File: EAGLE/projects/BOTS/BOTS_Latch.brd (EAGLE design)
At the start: 26.7 x 47 mm, 5 parts, among them J1 T821108A1S100CEU, K1 RT444012

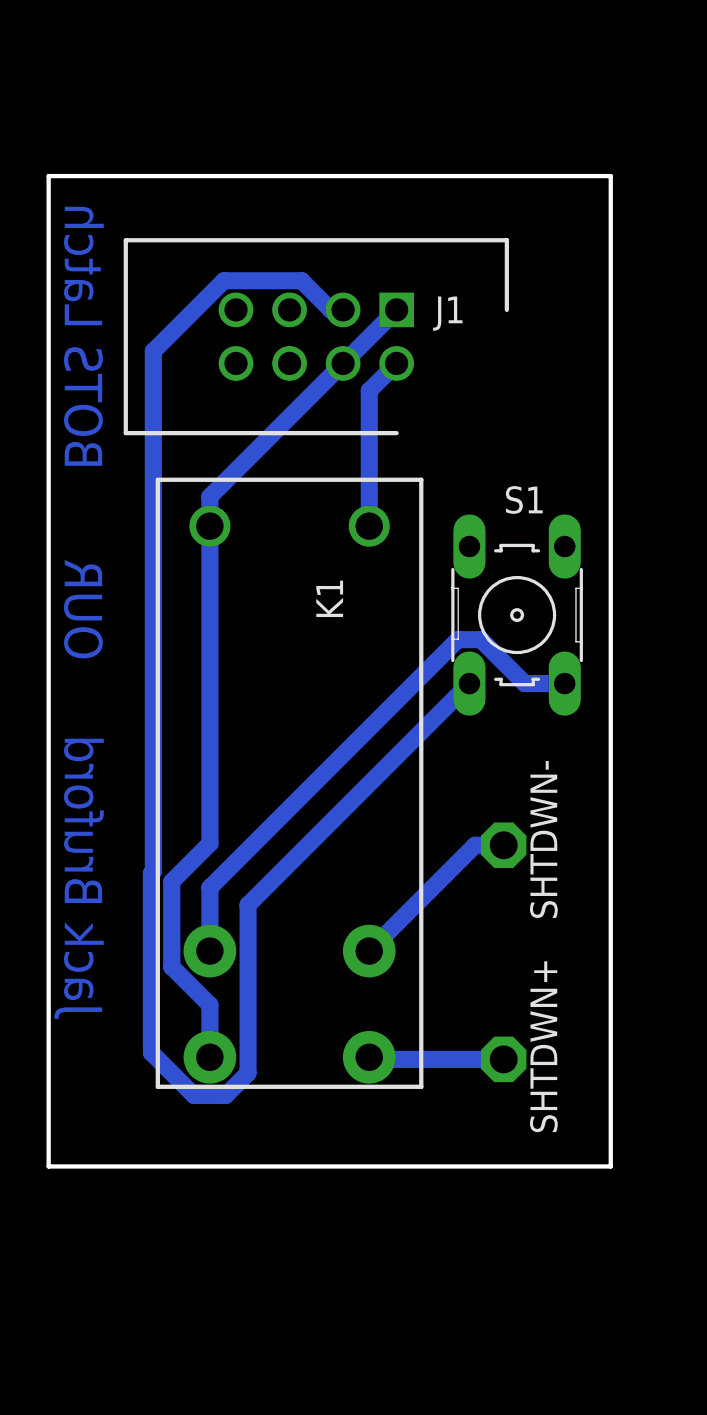
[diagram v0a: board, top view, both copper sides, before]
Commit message: Updates to BOTS circuit moving 12v pin to correct position and AMS circuit updates, including library for dual coil relay
Signed-off-by: Jack Bruford <jack.bruford41@gmail.com>
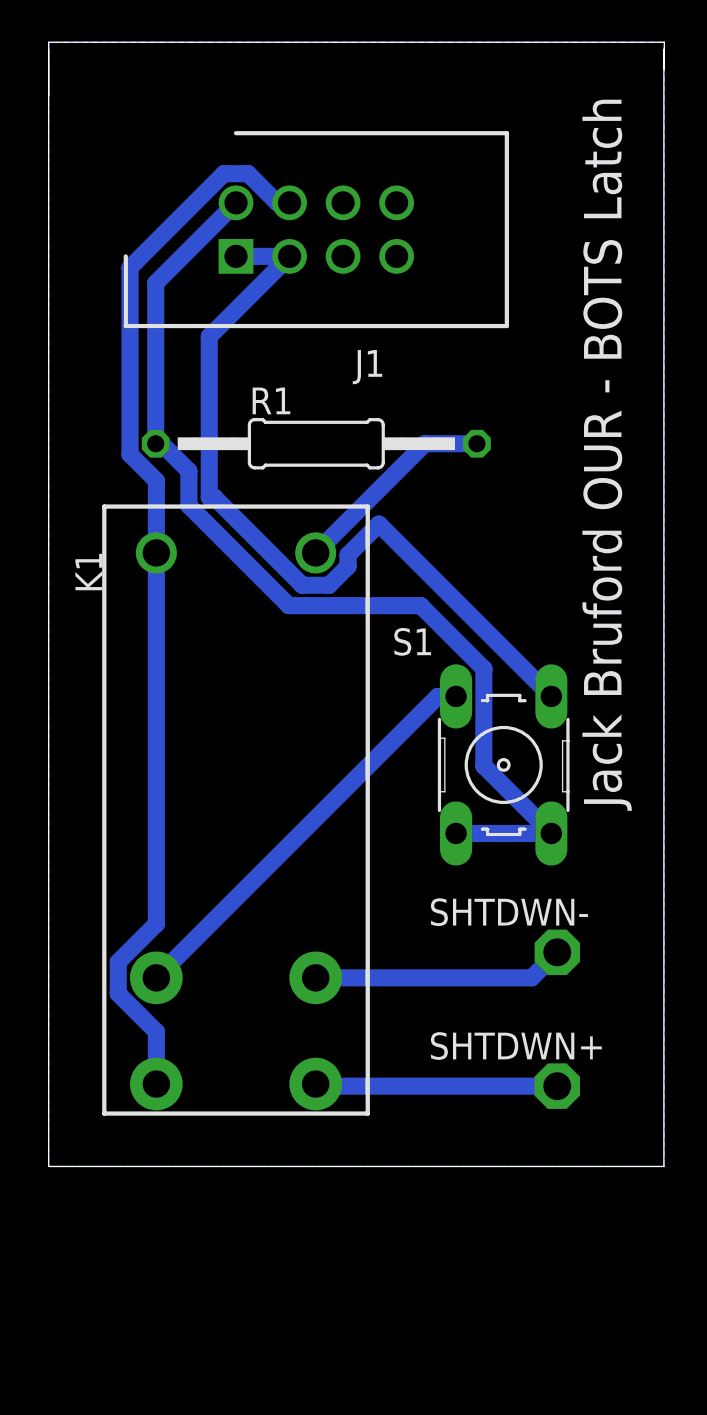
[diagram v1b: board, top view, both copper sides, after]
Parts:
- added R1: (no value), rcl:0207/15
- moved J1 8.03 mm to (8.89, 43.2), turned to 0 degrees
- moved S1 7.14 mm to (21.6, 19.1), turned to 90 degrees
- moved SHTDWN- 5.68 mm to (24.1, 10.2)
- moved K1 2.84 mm to (8.89, 16.5)
- moved SHTDWN+ 2.84 mm to (24.1, 3.81)
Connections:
- new net N$5: J1.4, K1.14, K1.A1
- net +12V: now also J1.3, S1.4; no longer J1.4, K1.14, K1.A1
- net GND: now also R1.1, S1.1, S1.3; no longer K1.A2
- net N$2: now also K1.A2, R1.2; no longer J1.3, S1.4
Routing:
- net N$2: track 73.0 -> 9.80 mm
- net N$5: track 0.00 -> 50.7 mm
- net GND: track 8.26 -> 47.6 mm
- net N$1: track 25.6 -> 19.7 mm
- net N$3: track 6.42 -> 11.5 mm
- net N$4: track 8.46 -> 12.0 mm
- net +12V: track 40.6 -> 38.4 mm
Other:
- board size 26.7 x 47 mm -> 29.2 x 53.3 mm
- board text added: "Jack Bruford OUR - BOTS Latch"
- board text removed: "Jack Bruford OUR BOTS Latch"

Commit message: BOTS revision so that ESDC goes through connector
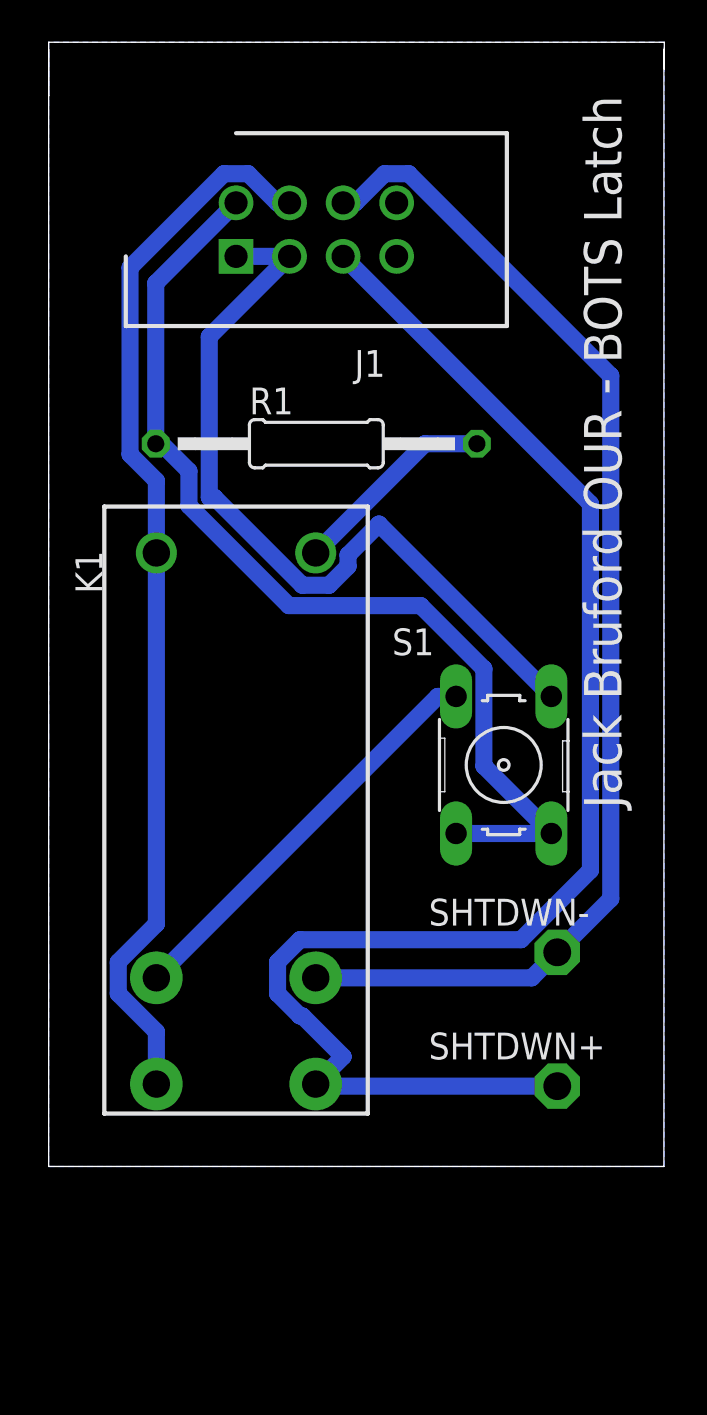
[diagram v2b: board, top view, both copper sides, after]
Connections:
- net N$3: now also J1.5
- net N$4: now also J1.6
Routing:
- net N$3: track 11.5 -> 69.8 mm
- net N$4: track 12.0 -> 57.6 mm
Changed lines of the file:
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@@
 <wire x1="12.67" y1="3.91" x2="12.77" y2="3.81" width="0.8128" layer="16"/>
 <wire x1="12.77" y1="3.81" x2="24.13" y2="3.81" width="0.8128" layer="16"/>
+<contactref element="J1" pad="5"/>
+<wire x1="13.97" y1="5.21" x2="12.67" y2="3.91" width="0.8128" layer="16"/>
+<wire x1="11.92076875" y1="10.7588" x2="10.8612" y2="9.69923125" width="0.8128" layer="16"/>
+<wire x1="10.8612" y1="9.69923125" x2="10.8612" y2="8.20076875" width="0.8128" layer="16"/>
+<wire x1="10.8612" y1="8.20076875" x2="11.92076875" y2="7.1412" width="0.8128" layer="16"/>
+<wire x1="11.92076875" y1="7.1412" x2="12.0388" y2="7.1412" width="0.8128" layer="16"/>
+<wire x1="12.0388" y1="7.1412" x2="13.97" y2="5.21" width="0.8128" layer="16"/>
+<wire x1="25.7048" y1="14.05170625" x2="22.41189375" y2="10.7588" width="0.8128" layer="16"/>
+<wire x1="22.41189375" y1="10.7588" x2="11.92076875" y2="10.7588" width="0.8128" layer="16"/>
+<wire x1="13.97" y1="43.18" x2="25.7048" y2="31.4452" width="0.8128" layer="16"/>
+<wire x1="25.7048" y1="31.4452" x2="25.7048" y2="14.05170625" width="0.8128" layer="16"/>
 </signal>
 <signal name="N$4">
@@
 <wire x1="12.67" y1="8.95" x2="22.92" y2="8.95" width="0.8128" layer="16"/>
 <wire x1="22.92" y1="8.95" x2="24.13" y2="10.16" width="0.8128" layer="16"/>
+<contactref element="J1" pad="6"/>
+<wire x1="15.93680625" y1="47.1038" x2="17.08319375" y2="47.1038" width="0.8128" layer="16"/>
+<wire x1="17.08319375" y1="47.1038" x2="26.67" y2="37.51699375" width="0.8128" layer="16"/>
+<wire x1="13.97" y1="45.72" x2="14.55300625" y2="45.72" width="0.8128" layer="16"/>
+<wire x1="14.55300625" y1="45.72" x2="15.93680625" y2="47.1038" width="0.8128" layer="16"/>
+<wire x1="26.67" y1="12.7" x2="24.13" y2="10.16" width="0.8128" layer="16"/>
+<wire x1="26.67" y1="37.51699375" x2="26.67" y2="12.7" width="0.8128" layer="16"/>
 </signal>
 <signal name="N$1">

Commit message: Update for workshop
Signed-off-by: Jack Bruford <jack.bruford41@gmail.com>
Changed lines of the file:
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@@
 <wire x1="7.860875" y1="31.75" x2="7.62" y2="31.75" width="0.8128" layer="16"/>
 <wire x1="12.034675" y1="27.5762" x2="7.860875" y2="31.75" width="0.8128" layer="16"/>
-<wire x1="7.62" y1="31.75" x2="7.62" y2="39.37" width="0.8128" layer="16"/>
-<wire x1="7.62" y1="39.37" x2="11.43" y2="43.18" width="0.8128" layer="16"/>
+<wire x1="7.62" y1="36.83" x2="7.62" y2="31.75" width="0.8128" layer="16"/>
 <wire x1="8.89" y1="43.18" x2="11.43" y2="43.18" width="0.8128" layer="16"/>
+<wire x1="11.43" y1="43.18" x2="11.43" y2="40.64" width="0.8128" layer="16"/>
+<wire x1="11.43" y1="40.64" x2="7.62" y2="36.83" width="0.8128" layer="16"/>
 </signal>
 <signal name="GND">
 <contactref element="J1" pad="2"/>
 <contactref element="R1" pad="1"/>
-<wire x1="5.08" y1="34.29" x2="5.08" y2="41.91" width="0.8128" layer="16"/>
-<wire x1="5.08" y1="41.91" x2="8.89" y2="45.72" width="0.8128" layer="16"/>
 <contactref element="S1" pad="1"/>
 <contactref element="S1" pad="3"/>
@@
 <vertex x="0" y="53.34"/>
 </polygon>
+<wire x1="8.89" y1="45.72" x2="7.874" y2="44.704" width="0.8128" layer="16"/>
+<wire x1="7.874" y1="44.704" x2="7.6933375" y2="44.704" width="0.8128" layer="16"/>
+<wire x1="7.6933375" y1="44.704" x2="5.08" y2="42.0906625" width="0.8128" layer="16"/>
+<wire x1="5.08" y1="42.0906625" x2="5.08" y2="34.29" width="0.8128" layer="16"/>
 </signal>
 <signal name="N$3">
@@
 <wire x1="22.92" y1="8.95" x2="24.13" y2="10.16" width="0.8128" layer="16"/>
 <contactref element="J1" pad="6"/>
-<wire x1="15.93680625" y1="47.1038" x2="17.08319375" y2="47.1038" width="0.8128" layer="16"/>
-<wire x1="17.08319375" y1="47.1038" x2="26.67" y2="37.51699375" width="0.8128" layer="16"/>
-<wire x1="13.97" y1="45.72" x2="14.55300625" y2="45.72" width="0.8128" layer="16"/>
-<wire x1="14.55300625" y1="45.72" x2="15.93680625" y2="47.1038" width="0.8128" layer="16"/>
 <wire x1="26.67" y1="12.7" x2="24.13" y2="10.16" width="0.8128" layer="16"/>
 <wire x1="26.67" y1="37.51699375" x2="26.67" y2="12.7" width="0.8128" layer="16"/>
+<wire x1="15.8787375" y1="47.244" x2="17.1412625" y2="47.244" width="0.8128" layer="16"/>
+<wire x1="17.1412625" y1="47.244" x2="18.034" y2="46.3512625" width="0.8128" layer="16"/>
+<wire x1="13.97" y1="45.72" x2="14.3547375" y2="45.72" width="0.8128" layer="16"/>
+<wire x1="18.034" y1="46.3512625" x2="18.034" y2="46.15299375" width="0.8128" layer="16"/>
+<wire x1="14.3547375" y1="45.72" x2="15.8787375" y2="47.244" width="0.8128" layer="16"/>
+<wire x1="18.034" y1="46.15299375" x2="26.67" y2="37.51699375" width="0.8128" layer="16"/>
 </signal>
 <signal name="N$1">
@@
 <wire x1="5.11" y1="6.39196875" x2="3.3012" y2="8.20076875" width="0.8128" layer="16"/>
 <wire x1="3.3012" y1="9.69923125" x2="5.11" y2="11.50803125" width="0.8128" layer="16"/>
-<wire x1="9.46319375" y1="47.1038" x2="8.31680625" y2="47.1038" width="0.8128" layer="16"/>
 <wire x1="5.11" y1="32.5357875" x2="5.11" y2="29.11" width="0.8128" layer="16"/>
 <wire x1="3.8608" y1="33.7849875" x2="5.11" y2="32.5357875" width="0.8128" layer="16"/>
-<wire x1="8.31680625" y1="47.1038" x2="3.8608" y2="42.64779375" width="0.8128" layer="16"/>
-<wire x1="3.8608" y1="42.64779375" x2="3.8608" y2="33.7849875" width="0.8128" layer="16"/>
-<wire x1="11.43" y1="45.72" x2="10.84699375" y2="45.72" width="0.8128" layer="16"/>
-<wire x1="10.84699375" y1="45.72" x2="9.46319375" y2="47.1038" width="0.8128" layer="16"/>
+<wire x1="9.5212625" y1="47.244" x2="8.2587375" y2="47.244" width="0.8128" layer="16"/>
+<wire x1="11.43" y1="45.72" x2="11.0452625" y2="45.72" width="0.8128" layer="16"/>
+<wire x1="11.0452625" y1="45.72" x2="9.5212625" y2="47.244" width="0.8128" layer="16"/>
+<wire x1="8.2587375" y1="47.244" x2="3.8608" y2="42.8460625" width="0.8128" layer="16"/>
+<wire x1="3.8608" y1="42.8460625" x2="3.8608" y2="33.7849875" width="0.8128" layer="16"/>
 </signal>
 <signal name="N$2">
